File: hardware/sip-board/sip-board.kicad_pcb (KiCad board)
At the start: 8 copper layers, 0 parts

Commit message: 3d model for fpga, part placement done(?)
Look into Xilinx programming adapters still. We do not have lots of space to work with.
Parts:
- added C1: 10u, Capacitor_SMD:C_0201_0603Metric, F.Cu at (104.2, 63.7)
- added C10: 0.47u, Capacitor_SMD:C_01005_0402Metric, B.Cu at (110.3, 76.4)
- added C11: 10u, Capacitor_SMD:C_0201_0603Metric, F.Cu at (113.3, 88.9)
- added C12: 0.47u, Capacitor_SMD:C_01005_0402Metric, B.Cu at (109.6, 73.2)
- added C13: 0.47u, Capacitor_SMD:C_01005_0402Metric, B.Cu at (108.8, 78.4)
- added C14: 100u, Capacitor_SMD:C_0201_0603Metric, F.Cu at (104.9, 69.6)
- added C15: 100u, Capacitor_SMD:C_0201_0603Metric, F.Cu at (108.5, 68.8)
- added C16: 4.7u, Capacitor_SMD:C_01005_0402Metric, B.Cu at (109.6, 75.2)
- added C17: 4.7u, Capacitor_SMD:C_01005_0402Metric, F.Cu at (107.2, 80.0)
- added C18: 4.7u, Capacitor_SMD:C_01005_0402Metric, B.Cu at (108.1, 74.7)
- added C19: 4.7u, Capacitor_SMD:C_01005_0402Metric, F.Cu at (109.9, 80.0)
- added C2: 50u, Capacitor_SMD:C_0201_0603Metric, F.Cu at (111.3, 63.7)
- added C20: 0.47u, Capacitor_SMD:C_01005_0402Metric, B.Cu at (107.3, 73.9)
- added C21: 0.47u, Capacitor_SMD:C_01005_0402Metric, B.Cu at (107.6, 75.2)
- added C22: 0.47u, Capacitor_SMD:C_01005_0402Metric, B.Cu at (110.3, 75.4)
- added C23: 0.47u, Capacitor_SMD:C_01005_0402Metric, B.Cu at (110.3, 74.4)
- added C24: 47u, Capacitor_SMD:C_0201_0603Metric, F.Cu at (112.2, 69.6)
- added C25: 100u, Capacitor_SMD:C_0201_0603Metric, F.Cu at (105.9, 79.8)
- added C26: 4.7u, Capacitor_SMD:C_01005_0402Metric, B.Cu at (110.1, 73.7)
- added C27: 4.7u, Capacitor_SMD:C_01005_0402Metric, F.Cu at (107.8, 69.6)
- added C28: 0.47u, Capacitor_SMD:C_01005_0402Metric, B.Cu at (109.1, 73.7)
- added C29: 4.7u, Capacitor_SMD:C_01005_0402Metric, F.Cu at (109.1, 69.6)
- added C3: 50u, Capacitor_SMD:C_0201_0603Metric, F.Cu at (107.7, 62.9)
- added C30: 0.47u, Capacitor_SMD:C_01005_0402Metric, B.Cu at (107.8, 73.4)
- added C31: 0.47u, Capacitor_SMD:C_01005_0402Metric, F.Cu at (107.8, 70.3)
- added C32: 0.47u, Capacitor_SMD:C_01005_0402Metric, F.Cu at (109.1, 70.3)
- added C33: 0.47u, Capacitor_SMD:C_01005_0402Metric, B.Cu at (110.3, 77.1)
- added C34: 0.47u, Capacitor_SMD:C_01005_0402Metric, B.Cu at (107.8, 76.9)
- added C35: 100u, Capacitor_SMD:C_0201_0603Metric, F.Cu at (110.9, 79.8)
- added C36: 4.7u, Capacitor_SMD:C_01005_0402Metric, F.Cu at (113.7, 78.8)
- added C37: 4.7u, Capacitor_SMD:C_01005_0402Metric, F.Cu at (113.7, 78.1)
- added C4: 1u, Capacitor_SMD:C_0201_0603Metric, F.Cu at (112.2, 68.0)
- added C5: 100u, Capacitor_SMD:C_0201_0603Metric, F.Cu at (108.5, 67.2)
- added C6: 1u, Capacitor_SMD:C_0201_0603Metric, F.Cu at (104.9, 68.0)
- added C7: 0.47u, Capacitor_SMD:C_01005_0402Metric, B.Cu at (109.6, 78.2)
- added C8: 0.47u, Capacitor_SMD:C_01005_0402Metric, B.Cu at (108.1, 78.2)
- added C9: 0.47u, Capacitor_SMD:C_01005_0402Metric, B.Cu at (108.6, 73.2)
- added CFG1: SW_DIP_x03, Button_Switch_SMD:SW_DIP_SPSTx03_Slide_6.7x9.18mm_W6.73mm_P2.54mm_LowProfile_JPin, F.Cu at (108.6, 94.7)
- added D3: LED, LED_SMD:LED_0201_0603Metric, F.Cu at (106.1, 68.5)
- added D4: LED, LED_SMD:LED_0201_0603Metric, F.Cu at (113.4, 68.5)
- added D5: LED, LED_SMD:LED_0201_0603Metric, F.Cu at (109.7, 67.7)
- added DONE1: LED, LED_SMD:LED_0201_0603Metric, F.Cu at (113.6, 80.2)
- added IC1: XC7S15-1CPGA196C, fpga_stuff:BGA196C50P14X14_800X800X110, F.Cu at (108.8, 75.2)
- added INIT1: LED, LED_SMD:LED_0201_0603Metric, F.Cu at (108.9, 80.7)
- added J1: Conn_01x05_Pin, Connector_PinHeader_2.54mm:PinHeader_1x05_P2.54mm_Vertical, F.Cu at (113.6, 52.0)
- added J2: Conn_01x10_Pin, Connector_PinHeader_2.54mm:PinHeader_1x10_P2.54mm_Vertical, F.Cu at (100.0, 50.9)
- added J3: Conn_01x10_Pin, Connector_PinHeader_2.54mm:PinHeader_1x10_P2.54mm_Vertical, F.Cu at (100.0, 76.2)
- added J4: Conn_01x10_Pin, Connector_PinHeader_2.54mm:PinHeader_1x10_P2.54mm_Vertical, F.Cu at (117.0, 76.2)
- added J5: Conn_01x10_Pin, Connector_PinHeader_2.54mm:PinHeader_1x10_P2.54mm_Vertical, F.Cu at (117.0, 50.9)
- added R1: 1k, Resistor_SMD:R_0201_0603Metric, F.Cu at (113.8, 97.5)
- added R10: 10k, Resistor_SMD:R_0201_0603Metric, B.Cu at (114.7, 62.6)
- added R11: 10k, Resistor_SMD:R_0201_0603Metric, B.Cu at (114.8, 73.3)
- added R12: 10k, Resistor_SMD:R_0201_0603Metric, B.Cu at (114.8, 82.6)
- added R13: 10k, Resistor_SMD:R_0201_0603Metric, B.Cu at (114.8, 93.1)
- added R14: 5k, Resistor_SMD:R_0201_0603Metric, F.Cu at (105.9, 80.7)
- added R16: 4k7, Resistor_SMD:R_0201_0603Metric, F.Cu at (108.9, 79.8)
- added R17: 5k7, Resistor_SMD:R_0201_0603Metric, F.Cu at (112.8, 80.2)
- added R18: 2k3, Resistor_SMD:R_0201_0603Metric, F.Cu at (104.9, 68.8)
- added R19: 3k, Resistor_SMD:R_0201_0603Metric, F.Cu at (112.2, 68.8)
- added R2: 1k, Resistor_SMD:R_0201_0603Metric, F.Cu at (113.8, 95.0)
- added R20: 5k7, Resistor_SMD:R_0201_0603Metric, F.Cu at (108.5, 68.0)
- added R3: 1k, Resistor_SMD:R_0201_0603Metric, F.Cu at (113.8, 92.5)
- added R4: 10k, Resistor_SMD:R_0201_0603Metric, B.Cu at (102.5, 57.1)
- added R5: 10k, Resistor_SMD:R_0201_0603Metric, B.Cu at (102.5, 67.0)
- added R6: 10k, Resistor_SMD:R_0201_0603Metric, B.Cu at (102.6, 78.0)
- added R7: 10k, Resistor_SMD:R_0201_0603Metric, B.Cu at (102.5, 87.3)
- added R8: 10k, Resistor_SMD:R_0201_0603Metric, B.Cu at (102.5, 97.7)
- added R9: 10k, Resistor_SMD:R_0201_0603Metric, B.Cu at (114.2, 53.4)
- added SW2: SW_RESET, Button_Switch_SMD:SW_Push_1P1T_NO_6x6mm_H9.5mm, F.Cu at (108.6, 84.9)
- added U1: TLV75718PDRV, Package_SON:WSON-6-1EP_2x2mm_P0.65mm_EP1x1.6mm, F.Cu at (112.0, 65.9)
- added U10: ~, hardware:NXB0104_XQFN12, B.Cu at (114.3, 53.8)
- added U11: ~, hardware:NXB0104_XQFN12, B.Cu at (114.3, 63.6)
- added U12: ~, hardware:NXB0104_XQFN12, B.Cu at (114.4, 74.5)
- added U13: ~, hardware:NXB0104_XQFN12, B.Cu at (114.4, 83.8)
- added U14: ~, hardware:NXB0104_XQFN12, B.Cu at (114.4, 94.1)
- added U15: AT25SF081-XMHD-X, Package_SO:TSSOP-8_4.4x3mm_P0.65mm, F.Cu at (108.4, 60.2)
- added U2: TLV75733PDRV, Package_SON:WSON-6-1EP_2x2mm_P0.65mm_EP1x1.6mm, F.Cu at (108.3, 65.1)
- added U3: TLV75710PDRV, Package_SON:WSON-6-1EP_2x2mm_P0.65mm_EP1x1.6mm, F.Cu at (104.9, 66.0)
- added U5: ~, hardware:NXB0104_XQFN12, B.Cu at (102.9, 56.5)
- added U6: ~, hardware:NXB0104_XQFN12, B.Cu at (102.9, 66.4)
- added U7: ~, hardware:NXB0104_XQFN12, B.Cu at (103.0, 77.3)
- added U8: ~, hardware:NXB0104_XQFN12, B.Cu at (103.0, 86.5)
- added U9: ~, hardware:NXB0104_XQFN12, B.Cu at (103.0, 96.8)
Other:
- board outline added: 17 x 50 mm
- board text added: "+5V"
- board text added: "1V0"
- board text added: "1V8"
- board text added: "3V3"
- board text added: "3V3 (provided)"
- board text added: "A 1 0"
- board text added: "A 1 1"
- board text added: "A0"
- board text added: "A1"
- board text added: "A12"
- board text added: "A13"
- board text added: "A14"
- board text added: "A15"
- board text added: "A2"
- board text added: "A3"
- board text added: "A4"
- board text added: "A5"
- board text added: "A6"
- board text added: "A7"
- board text added: "A8"
- board text added: "A9"
- board text added: "BUSAK"
- board text added: "BUSRQ"
- board text added: "CLK"
- board text added: "D0"
- board text added: "D1"
- board text added: "D2"
- board text added: "D3"
- board text added: "D4"
- board text added: "D5"
- board text added: "D6"
- board text added: "D7"
- board text added: "FIGURE OUT WHAT LEDS WE ARE USING AND CHANGE RESISTOR VALUES!"
- board text added: "GND"
- board text added: "HALT"
- board text added: "INT"
- board text added: "IORQ"
- board text added: "M1"
- board text added: "MREQ"
- board text added: "M[2:0] = 001 SPI M[2:0] = 101 JTAG"
- board text added: "Must be plugged into 5V on board or power supply providing 5V to correct pin (see left) to program."
- board text added: "NMI"
- board text added: "RD"
- board text added: "RESET"
- board text added: "RFSH"
- board text added: "RST"
- board text added: "TCK"
- board text added: "TDI"
- board text added: "TDO"
- board text added: "TMS"
- board text added: "Top left corner of board is (100, 50)"
- board text added: "WAIT"
- board text added: "WR"

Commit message: fix the paths (again)
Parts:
- removed J1: Conn_01x05_Pin, Connector_PinHeader_2.54mm:PinHeader_1x05_P2.54mm_Vertical
- removed U15: AT25SF081-XMHD-X, Package_SO:TSSOP-8_4.4x3mm_P0.65mm
- added C38: 10u, Capacitor_SMD:C_0402_1005Metric, F.Cu at (26.1, 61.9)
- added IC2: MT25QL512ABB1EW9-0SIT, hardware:MT25QL512ABB1EW9-0SIT, F.Cu at (32.7, 58.5)
- added JTAG1: Conn_01x06_Pin, Connector_PinHeader_2.54mm:PinHeader_1x06_P2.54mm_Vertical, F.Cu at (45.6, 48.5)
- added R15: 5k, Resistor_SMD:R_0201_0603Metric, F.Cu at (54.3, 45.3)
- added R21: 5k, Resistor_SMD:R_0201_0603Metric, F.Cu at (56.8, 40.1)
- C1, C14, C15, C2, C25, C3, C5: footprint Capacitor_SMD:C_0201_0603Metric -> Capacitor_SMD:C_0402_1005Metric
- C10, C12, C13, C16, C18, C20, C21, C22, C23, C26, C28, C30, C33, C34, C7, C8, C9: footprint Capacitor_SMD:C_01005_0402Metric -> Capacitor_SMD:C_0201_0603Metric; moved to F.Cu
- C17, C19, C27, C29, C31, C32, C36, C37: footprint Capacitor_SMD:C_01005_0402Metric -> Capacitor_SMD:C_0201_0603Metric
- R10, R11, R12, R13, R4, R5, R6, R7, R8, R9: moved to F.Cu
- U10, U11, U12, U13, U14, U5, U6, U7, U8, U9: footprint hardware:NXB0104_XQFN12 -> hardware:NXB0104GU12X; moved to F.Cu
- moved J4 97.3 mm to (36.3, 22.0)
- moved J3 87.3 mm to (31.6, 22.0)
- moved R1 86.9 mm to (51.9, 36.6), turned to 0 degrees
- moved C2 86.3 mm to (26.1, 50.1), turned to 0 degrees
- moved R2 84.0 mm to (51.9, 38.3), turned to 0 degrees
- moved C5 83.4 mm to (26.1, 54.0)
- moved C11 83.4 mm to (44.5, 41.8), turned to 0 degrees
- moved C15 83.1 mm to (26.1, 58.0)
- moved U9 83.0 mm to (66.2, 22.3), turned to 0 degrees
- moved SW2 82.9 mm to (33.1, 50.9)
- moved C3 82.3 mm to (26.1, 52.1), turned to 0 degrees
- moved C25 82.2 mm to (26.1, 60.0), turned to 0 degrees
- moved U14 82.0 mm to (66.2, 27.7)
- moved J5 81.3 mm to (41.0, 22.0)
- moved R3 81.2 mm to (51.9, 40.1), turned to 0 degrees
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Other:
- board outline removed
- board text removed: "+5V"
- board text removed: "1V0"
- board text removed: "1V8"
- board text removed: "3V3"
- board text removed: "3V3 (provided)"
- board text removed: "A 1 0"
- board text removed: "A 1 1"
- board text removed: "A0"
- board text removed: "A1"
- board text removed: "A12"
- board text removed: "A13"
- board text removed: "A14"
- board text removed: "A15"
- board text removed: "A2"
- board text removed: "A3"
- board text removed: "A4"
- board text removed: "A5"
- board text removed: "A6"
- board text removed: "A7"
- board text removed: "A8"
- board text removed: "A9"
- board text removed: "BUSAK"
- board text removed: "BUSRQ"
- board text removed: "CLK"
- board text removed: "D0"
- board text removed: "D1"
- board text removed: "D2"
- board text removed: "D3"
- board text removed: "D4"
- board text removed: "D5"
- board text removed: "D6"
- board text removed: "D7"
- board text removed: "FIGURE OUT WHAT LEDS WE ARE USING AND CHANGE RESISTOR VALUES!"
- board text removed: "GND"
- board text removed: "HALT"
- board text removed: "INT"
- board text removed: "IORQ"
- board text removed: "M1"
- board text removed: "MREQ"
- board text removed: "M[2:0] = 001 SPI M[2:0] = 101 JTAG"
- board text removed: "Must be plugged into 5V on board or power supply providing 5V to correct pin (see left) to program."
- board text removed: "NMI"
- board text removed: "RD"
- board text removed: "RESET"
- board text removed: "RFSH"
- board text removed: "RST"
- board text removed: "TCK"
- board text removed: "TDI"
- board text removed: "TDO"
- board text removed: "TMS"
- board text removed: "Top left corner of board is (100, 50)"
- board text removed: "WAIT"
- board text removed: "WR"

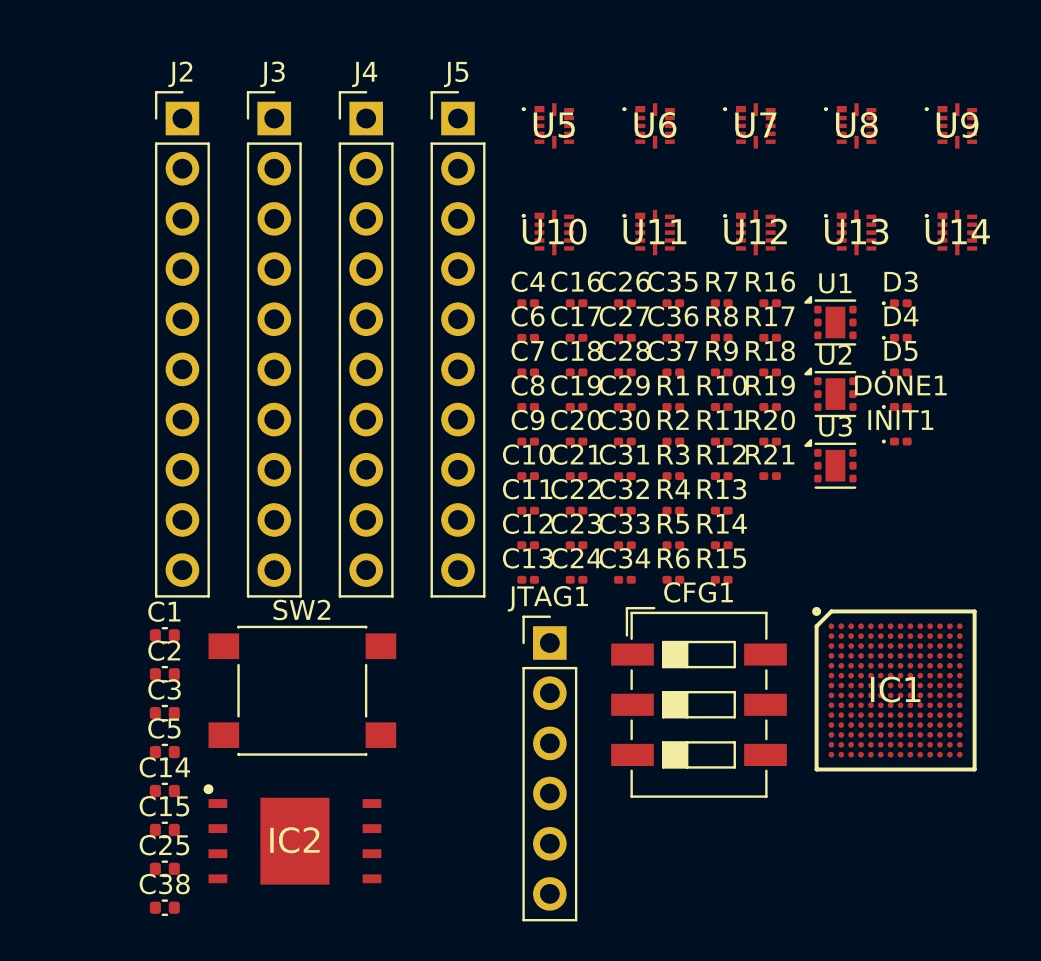
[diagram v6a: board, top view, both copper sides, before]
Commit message: add new parts: button, jtag connector
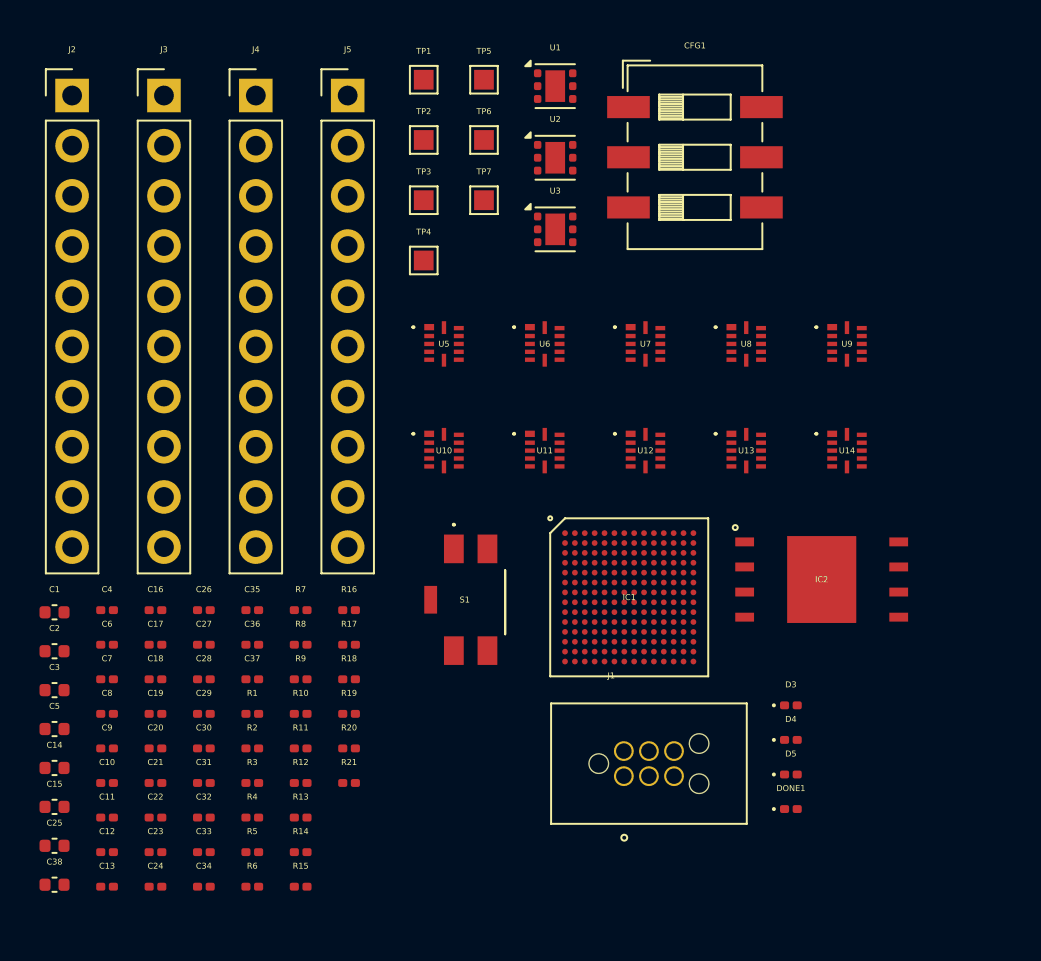
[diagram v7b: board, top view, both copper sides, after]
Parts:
- removed INIT1: LED, LED_SMD:LED_0201_0603Metric
- removed JTAG1: Conn_01x06_Pin, Connector_PinHeader_2.54mm:PinHeader_1x06_P2.54mm_Vertical
- removed SW2: SW_RESET, Button_Switch_SMD:SW_Push_1P1T_NO_6x6mm_H9.5mm
- added J1: Conn_02x03_Odd_Even, hardware:TAG_TC2030-IDC-NL, F.Cu at (50.6, 54.6)
- added S1: EVQ-P2R02W, hardware:EVQP2R02W, F.Cu at (41.6, 46.3)
- added TP1: TestPoint, TestPoint:TestPoint_Pad_1.0x1.0mm, F.Cu at (39.2, 20.0)
- added TP2: TestPoint, TestPoint:TestPoint_Pad_1.0x1.0mm, F.Cu at (39.2, 23.1)
- added TP3: TestPoint, TestPoint:TestPoint_Pad_1.0x1.0mm, F.Cu at (39.2, 26.1)
- added TP4: TestPoint, TestPoint:TestPoint_Pad_1.0x1.0mm, F.Cu at (39.2, 29.2)
- added TP5: TestPoint, TestPoint:TestPoint_Pad_1.0x1.0mm, F.Cu at (42.3, 20.0)
- added TP6: TestPoint, TestPoint:TestPoint_Pad_1.0x1.0mm, F.Cu at (42.3, 23.1)
- added TP7: TestPoint, TestPoint:TestPoint_Pad_1.0x1.0mm, F.Cu at (42.3, 26.1)
- R14, R15, R21: value 5k -> 4k7
- R17: value 5k7 -> 4k7
- moved IC2 29.8 mm to (59.4, 45.3)
- moved CFG1 27.7 mm to (52.9, 23.9)
- moved C10 26.4 mm to (23.2, 55.6)
- moved C11 26.4 mm to (23.2, 57.4)
- moved C12 26.4 mm to (23.2, 59.1)
- moved C13 26.4 mm to (23.2, 60.9)
- moved C16 26.4 mm to (25.6, 46.9)
- moved C17 26.4 mm to (25.6, 48.6)
- moved C18 26.4 mm to (25.6, 50.4)
- moved C19 26.4 mm to (25.6, 52.1)
- moved C20 26.4 mm to (25.6, 53.9)
- moved C21 26.4 mm to (25.6, 55.6)
- moved C22 26.4 mm to (25.6, 57.4)
- moved C23 26.4 mm to (25.6, 59.1)
- moved C24 26.4 mm to (25.6, 60.9)
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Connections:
- net Net-(IC1-INIT_B_0) renamed INIT_B
- net SPI_SCK renamed SPI_SCK_CCLK
- DONE1 pad 2: Net-(DONE1-A) -> DONE
- IC1 pad B10: GND -> +3V3
- IC2 pad 7: SPI_DQ0 -> SPI_DQ3
- R16 pad 1: Net-(INIT1-A) -> +3V3
- R17 pad 1: DONE -> +3V3
- R17 pad 2: Net-(DONE1-A) -> SPI_DQ3
